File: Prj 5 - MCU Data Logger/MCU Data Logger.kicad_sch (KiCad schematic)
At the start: 25 parts, among them U1 24LC1025, U2 DS1337S+, U3 24LC1025, U4 ATmega328P, Y1 32.768KHz, Y2 16MHz

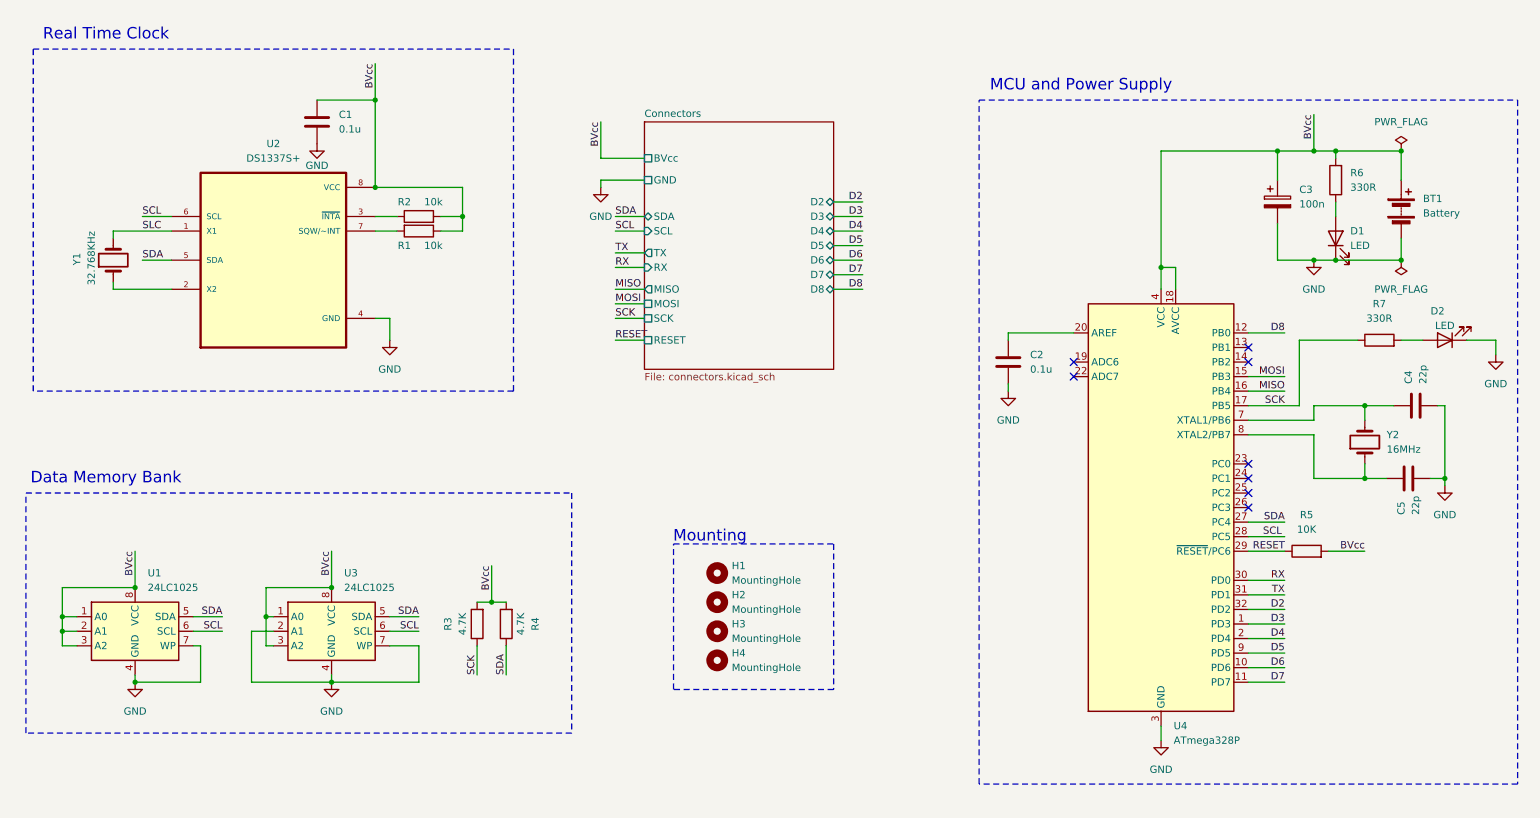
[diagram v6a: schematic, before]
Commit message: Separated SCL and SCK
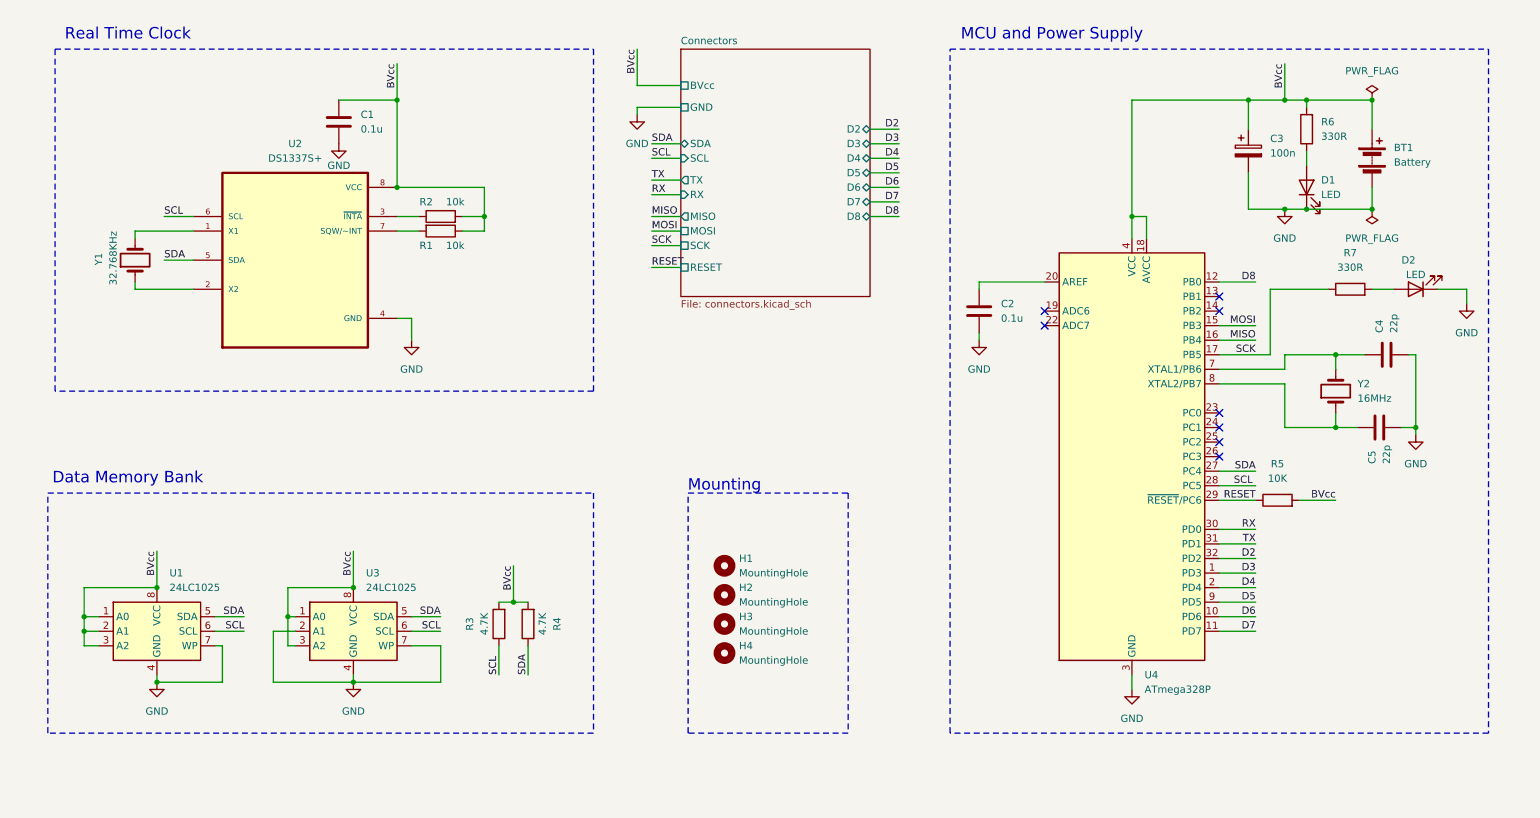
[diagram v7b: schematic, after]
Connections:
- net SCK: no longer R3.1
- net SCL: now also R3.1
- net SLC: no longer names the net of U2.1 (X1), Y1.2
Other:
- moved on the sheet: BT1, C1, C2, C3, C4, C5, D1, D2, H1, H2, H3, H4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
